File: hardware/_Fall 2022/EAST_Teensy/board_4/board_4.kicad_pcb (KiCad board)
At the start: 2 copper layers, 76.2 x 66.7 mm, 8 parts, among them J1 Conn_01x04, J2 Conn_02x09_Odd_Even, U1 Teensy4.1

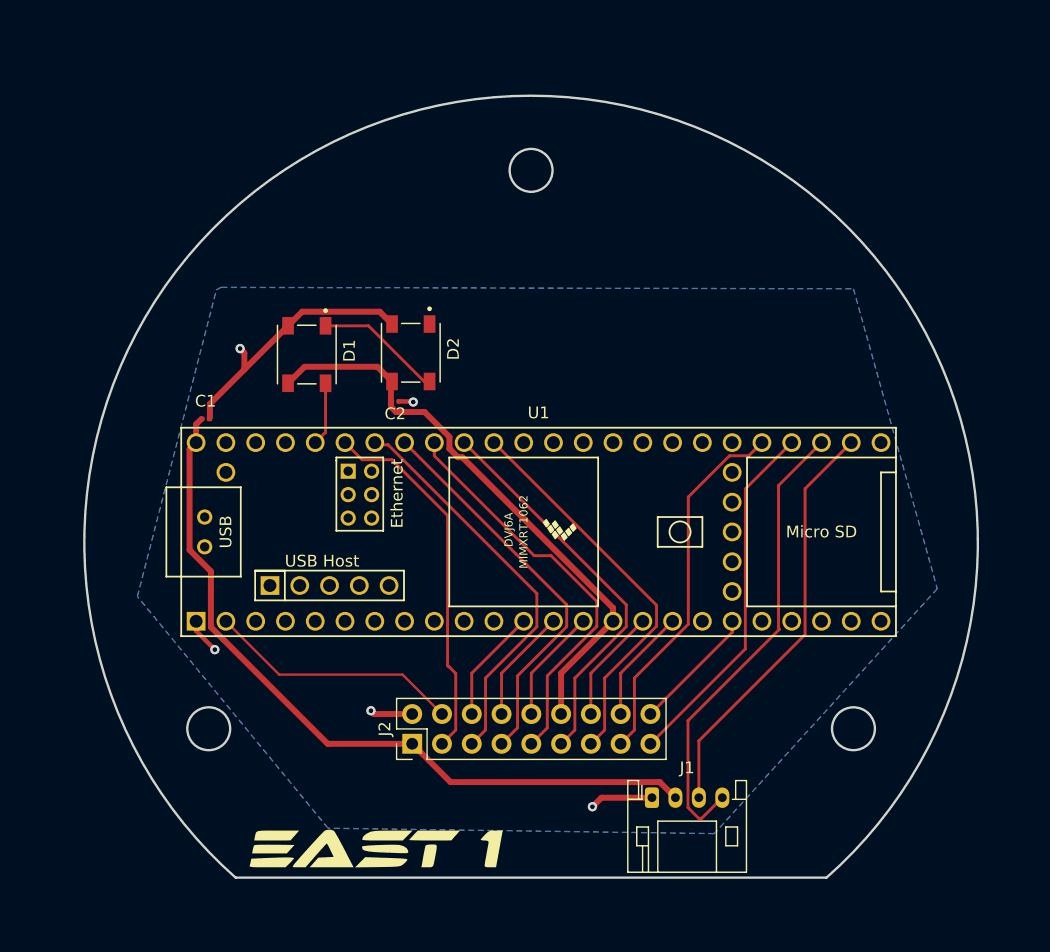
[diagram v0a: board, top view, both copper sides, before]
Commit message: add plated holes to both east boards
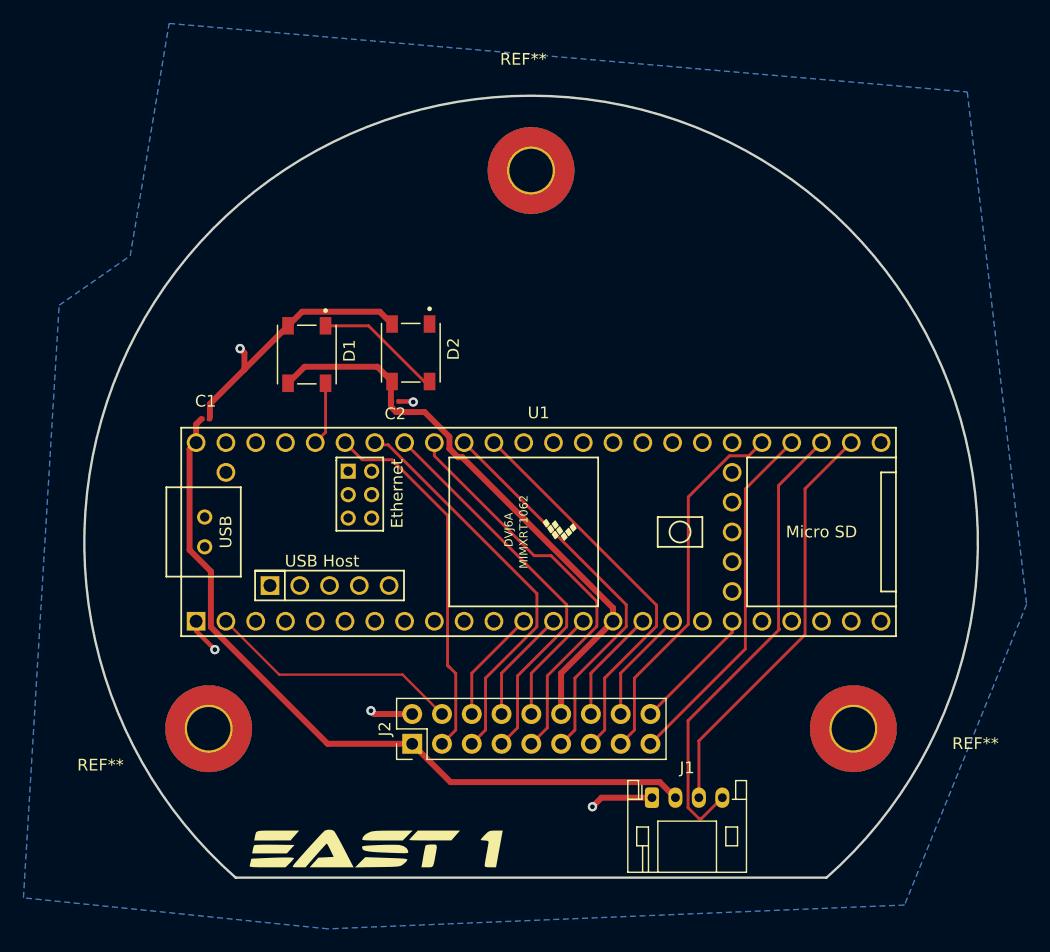
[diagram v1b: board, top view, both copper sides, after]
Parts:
- added REF**: MountingHole_3.7mm_Pad_TopBottom, MountingHole:MountingHole_3.7mm_Pad_TopBottom, F.Cu at (175.5, 139.4)
- added REF**: MountingHole_3.7mm_Pad_TopBottom, MountingHole:MountingHole_3.7mm_Pad_TopBottom, F.Cu at (148.0, 91.8)
- added REF**: MountingHole_3.7mm_Pad_TopBottom, MountingHole:MountingHole_3.7mm_Pad_TopBottom, F.Cu at (120.5, 139.4)
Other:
- outline, holes or cut-outs redrawn
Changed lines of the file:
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@@
   (net 68 "unconnected-(D2-Pad1)")
   (net 69 "unconnected-(U1-Pad23)")
+  (footprint "MountingHole:MountingHole_3.7mm_Pad_TopBottom" (layer "F.Cu")
+    (at 175.468013 139.389531)
+    (descr "Mounting Hole 3.7mm")
+    (tags "mounting hole 3.7mm")
+    (attr exclude_from_pos_files exclude_from_bom)
+    (fp_text reference "REF**" (at 10.414 1.27) (layer "F.SilkS")
+      (effects (font (size 1 1) (thickness 0.15)))
+    )
+    (fp_text value "MountingHole_3.7mm_Pad_TopBottom" (at 0 4.7) (layer "F.Fab")
+      (effects (font (size 1 1) (thickness 0.15)))
+    )
+    (fp_text user "${REFERENCE}" (at 0 0) (layer "F.Fab")
+      (effects (font (size 1 1) (thickness 0.15)))
+    )
+    (fp_circle (center 0 0) (end 3.7 0) (layer "Cmts.User") (width 0.15) (fill none))
+    (fp_circle (center 0 0) (end 3.95 0) (layer "F.CrtYd") (width 0.05) (fill none))
+    (pad "1" thru_hole circle (at 0 0) (size 4.1 4.1) (drill 3.7) (layers *.Cu *.Mask))
+    (pad "1" connect circle (at 0 0) (size 7.4 7.4) (layers "F.Cu" "F.Mask"))
+    (pad "1" connect circle (at 0 0) (size 7.4 7.4) (layers "B.Cu" "B.Mask"))
+  )
   (footprint "LOGO" (layer "F.Cu")
     (at 134.62 149.86)
@@
       (rotate (xyz 0 0 0))
     )
+  )
+  (footprint "MountingHole:MountingHole_3.7mm_Pad_TopBottom" (layer "F.Cu")
+    (at 147.976228 91.782125)
+    (descr "Mounting Hole 3.7mm")
+    (tags "mounting hole 3.7mm")
+    (attr exclude_from_pos_files exclude_from_bom)
+    (fp_text reference "REF**" (at -0.656228 -9.486125) (layer "F.SilkS")
+      (effects (font (size 1 1) (thickness 0.15)))
+    )
+    (fp_text value "MountingHole_3.7mm_Pad_TopBottom" (at 0 4.7) (layer "F.Fab")
+      (effects (font (size 1 1) (thickness 0.15)))
+    )
+    (fp_text user "${REFERENCE}" (at 0 0) (layer "F.Fab")
+      (effects (font (size 1 1) (thickness 0.15)))
+    )
+    (fp_circle (center 0 0) (end 3.7 0) (layer "Cmts.User") (width 0.15) (fill none))
+    (fp_circle (center 0 0) (end 3.95 0) (layer "F.CrtYd") (width 0.05) (fill none))
+    (pad "1" thru_hole circle (at 0 0) (size 4.1 4.1) (drill 3.7) (layers *.Cu *.Mask))
+    (pad "1" connect circle (at 0 0) (size 7.4 7.4) (layers "F.Cu" "F.Mask"))
+    (pad "1" connect circle (at 0 0) (size 7.4 7.4) (layers "B.Cu" "B.Mask"))
   )
   (footprint "Teensy:Teensy41" (layer "F.Cu")
@@
       (net 3 "Net-(D1-Pad1)") (pinfunction "DIN") (pintype "input"))
   )
+  (footprint "MountingHole:MountingHole_3.7mm_Pad_TopBottom" (layer "F.Cu")
+    (at 120.480277 139.392743)
+    (descr "Mounting Hole 3.7mm")
+    (tags "mounting hole 3.7mm")
+    (attr exclude_from_pos_files exclude_from_bom)
+    (fp_text reference "REF**" (at -9.228277 3.101257) (layer "F.SilkS")
+      (effects (font (size 1 1) (thickness 0.15)))
+    )
+    (fp_text value "MountingHole_3.7mm_Pad_TopBottom" (at 0 4.7) (layer "F.Fab")
+      (effects (font (size 1 1) (thickness 0.15)))
+    )
+    (fp_text user "${REFERENCE}" (at 0 0) (layer "F.Fab")
+      (effects (font (size 1 1) (thickness 0.15)))
+    )
+    (fp_circle (center 0 0) (end 3.7 0) (layer "Cmts.User") (width 0.15) (fill none))
+    (fp_circle (center 0 0) (end 3.95 0) (layer "F.CrtYd") (width 0.05) (fill none))
+    (pad "1" thru_hole circle (at 0 0) (size 4.1 4.1) (drill 3.7) (layers *.Cu *.Mask))
+    (pad "1" connect circle (at 0 0) (size 7.4 7.4) (layers "F.Cu" "F.Mask"))
+    (pad "1" connect circle (at 0 0) (size 7.4 7.4) (layers "B.Cu" "B.Mask"))
+  )
   (footprint "Capacitor_SMD:C_0201_0603Metric" (layer "F.Cu")
     (at 120.225 112.975)
@@
     (pad "18" thru_hole oval (at 2.54 20.32 90) (size 1.7 1.7) (drill 1) (layers *.Cu *.Mask)
       (net 9 "/SCK 1") (pinfunction "Pin_18") (pintype "passive"))
-    (model "${KICAD6_3DMODEL_DIR}/Connector_PinHeader_2.54mm.3dshapes/PinHeader_2x09_P2.54mm_Vertical.wrl"
+    (model "${KICAD6_3DMODEL_DIR}/Connector_PinHeader_2.54mm.3dshapes/PinHeader_2x09_P2.54mm_Vertical.wrl" hide
       (offset (xyz 0 0 0))
+      (scale (xyz 1 1 1))
+      (rotate (xyz 0 0 0))
+    )
+    (model "${KICAD6_3DMODEL_DIR}/Connector_PinSocket_2.54mm.3dshapes/PinSocket_2x09_P2.54mm_Vertical.step"
+      (offset (xyz 2.5 0 0))
       (scale (xyz 1 1 1))
       (rotate (xyz 0 0 0))
@@
   (gr_line (start 155.8204 143.4952) (end 166.7204 143.4952) (layer "Dwgs.User") (width 0.2))
   (gr_line (start 159.4104 141.9352) (end 136.5504 136.8552) (layer "Dwgs.User") (width 0.2))
+  (gr_circle (center 175.4759 139.394734) (end 177.3047 139.394734) (layer "Dwgs.User") (width 0.2) (fill none))
   (gr_line (start 166.7204 152.0952) (end 155.8204 152.0952) (layer "Dwgs.User") (width 0.2))
   (gr_line (start 136.5504 136.8552) (end 159.4104 136.8552) (layer "Dwgs.User") (width 0.2))
   (gr_line (start 147.9804 152.0952) (end 147.9804 139.3952) (layer "Dwgs.User") (width 0.2))
+  (gr_circle (center 147.9804 91.771131) (end 149.8092 91.771131) (layer "Dwgs.User") (width 0.2) (fill none))
+  (gr_circle (center 120.4849 139.394734) (end 122.3137 139.394734) (layer "Dwgs.User") (width 0.2) (fill none))
   (gr_line (start 159.4104 136.8552) (end 159.4104 141.9352) (layer "Dwgs.User") (width 0.2))
   (gr_line (start 161.2704 143.4952) (end 161.2704 152.0952) (layer "Dwgs.User") (width 0.2))
-  (gr_circle (center 175.4759 139.394734) (end 177.3047 139.394734) (layer "Edge.Cuts") (width 0.2) (fill none))
   (gr_line (start 122.779619 152.0952) (end 173.181181 152.0952) (layer "Edge.Cuts") (width 0.2))
-  (gr_circle (center 147.9804 91.771131) (end 149.8092 91.771131) (layer "Edge.Cuts") (width 0.2) (fill none))
-  (gr_circle (center 120.4849 139.394734) (end 122.3137 139.394734) (layer "Edge.Cuts") (width 0.2) (fill none))
   (gr_arc (start 122.779619 152.0952) (mid 147.9804 85.403268) (end 173.181181 152.0952) (layer "Edge.Cuts") (width 0.2))
   (segment (start 137.84 140.68) (end 130.626576 140.68) (width 0.508) (layer "F.Cu") (net 1))
@@
   (segment (start 158.16 140.68) (end 166.255 132.585) (width 0.25) (layer "F.Cu") (net 63))
   (zone (net 2) (net_name "GND") (layer "B.Cu") (hatch edge 0.508)
-    (connect_pads (clearance 0.508))
+    (connect_pads (clearance 1))
     (min_thickness 0.254) (filled_areas_thickness no)
     (fill yes (thermal_gap 0.508) (thermal_bridge_width 0.508))
     (polygon
       (pts
-        (xy 121.56 101.75)
-        (xy 175.474371 101.874481)
-        (xy 182.626 127.4572)
-        (xy 163.6 148.34)
-        (xy 130.66 147.88)
-        (xy 114.4016 128.1176)
-        (xy 121.14 101.96)
-        (xy 121.54 101.75)
+        (xy 117.109861 79.239885)
+        (xy 185.181861 85.081885)
+        (xy 190.246 128.778)
+        (xy 179.832 154.432)
+        (xy 130.66 156.464)
+        (xy 104.682416 153.81886)
+        (xy 107.730416 103.27286)
+        (xy 113.792 99.06)
       )
     )

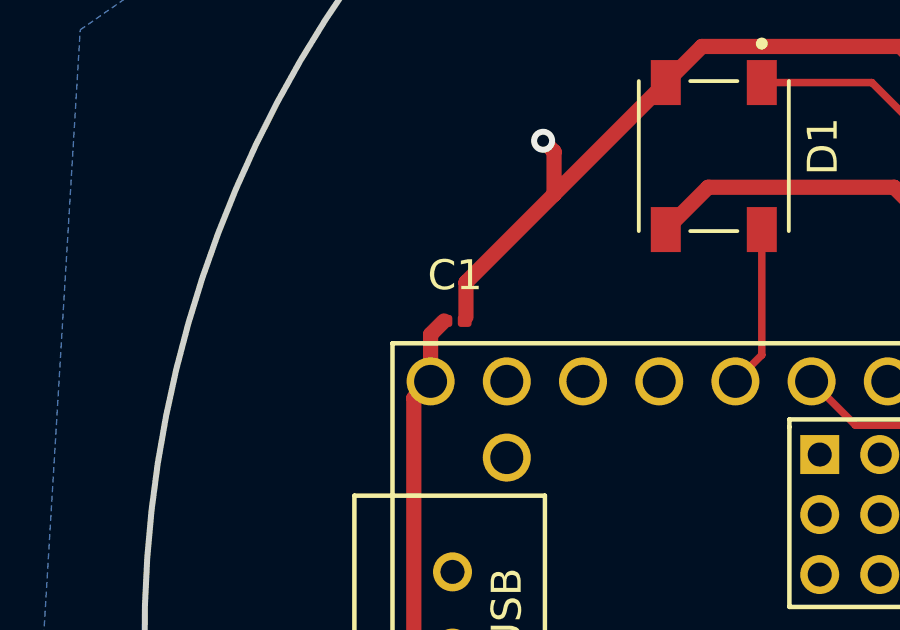
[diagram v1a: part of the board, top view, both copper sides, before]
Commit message: change board 4 C size and GPS labels hided
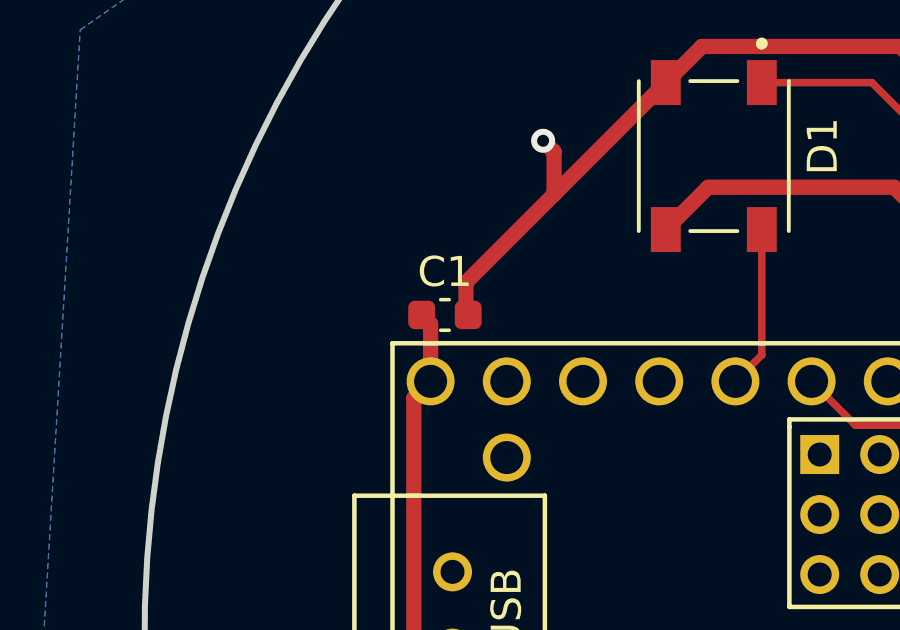
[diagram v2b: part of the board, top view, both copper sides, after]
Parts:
- C1: footprint Capacitor_SMD:C_0201_0603Metric -> Capacitor_SMD:C_0603_1608Metric
- moved C1 0.39 mm to (119.9, 112.8)
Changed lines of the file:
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@@
     (fp_circle (center 0 0) (end 3.7 0) (layer "Cmts.User") (width 0.15) (fill none))
     (fp_circle (center 0 0) (end 3.95 0) (layer "F.CrtYd") (width 0.05) (fill none))
+    (pad "1" connect circle (at 0 0) (size 7.4 7.4) (layers "B.Cu" "B.Mask"))
+    (pad "1" connect circle (at 0 0) (size 7.4 7.4) (layers "F.Cu" "F.Mask"))
     (pad "1" thru_hole circle (at 0 0) (size 4.1 4.1) (drill 3.7) (layers *.Cu *.Mask))
-    (pad "1" connect circle (at 0 0) (size 7.4 7.4) (layers "F.Cu" "F.Mask"))
-    (pad "1" connect circle (at 0 0) (size 7.4 7.4) (layers "B.Cu" "B.Mask"))
   )
   (footprint "Teensy:Teensy41" (layer "F.Cu")
@@
     (fp_circle (center 0 0) (end 3.7 0) (layer "Cmts.User") (width 0.15) (fill none))
     (fp_circle (center 0 0) (end 3.95 0) (layer "F.CrtYd") (width 0.05) (fill none))
+    (pad "1" connect circle (at 0 0) (size 7.4 7.4) (layers "B.Cu" "B.Mask"))
     (pad "1" thru_hole circle (at 0 0) (size 4.1 4.1) (drill 3.7) (layers *.Cu *.Mask))
     (pad "1" connect circle (at 0 0) (size 7.4 7.4) (layers "F.Cu" "F.Mask"))
-    (pad "1" connect circle (at 0 0) (size 7.4 7.4) (layers "B.Cu" "B.Mask"))
-  )
-  (footprint "Capacitor_SMD:C_0201_0603Metric" (layer "F.Cu")
-    (at 120.225 112.975)
-    (descr "Capacitor SMD 0201 (0603 Metric), square (rectangular) end terminal, IPC_7351 nominal, (Body size source: https://www.vishay.com/docs/20052/crcw0201e3.pdf), generated with kicad-footprint-generator")
+  )
+  (footprint "Capacitor_SMD:C_0603_1608Metric" (layer "F.Cu")
+    (at 119.888 112.776)
+    (descr "Capacitor SMD 0603 (1608 Metric), square (rectangular) end terminal, IPC_7351 nominal, (Body size source: IPC-SM-782 page 76, https://www.pcb-3d.com/wordpress/wp-content/uploads/ipc-sm-782a_amendment_1_and_2.pdf), generated with kicad-footprint-generator")
     (tags "capacitor")
     (property "JLC" "C307380")
@@
     (property "Sheetname" "")
     (attr smd)
-    (fp_text reference "C1" (at 0 -1.52) (layer "F.SilkS")
-      (effects (font (size 1 1) (thickness 0.15)))
-    )
-    (fp_text value "0.1uF" (at 0 1.05) (layer "F.Fab")
-      (effects (font (size 1 1) (thickness 0.15)))
-    )
-    (fp_text user "${REFERENCE}" (at 0 -0.68) (layer "F.Fab")
-      (effects (font (size 0.25 0.25) (thickness 0.04)))
-    )
-    (fp_line (start -0.7 -0.35) (end 0.7 -0.35) (layer "F.CrtYd") (width 0.05))
-    (fp_line (start 0.7 0.35) (end -0.7 0.35) (layer "F.CrtYd") (width 0.05))
-    (fp_line (start 0.7 -0.35) (end 0.7 0.35) (layer "F.CrtYd") (width 0.05))
-    (fp_line (start -0.7 0.35) (end -0.7 -0.35) (layer "F.CrtYd") (width 0.05))
-    (fp_line (start 0.3 0.15) (end -0.3 0.15) (layer "F.Fab") (width 0.1))
-    (fp_line (start 0.3 -0.15) (end 0.3 0.15) (layer "F.Fab") (width 0.1))
-    (fp_line (start -0.3 -0.15) (end 0.3 -0.15) (layer "F.Fab") (width 0.1))
-    (fp_line (start -0.3 0.15) (end -0.3 -0.15) (layer "F.Fab") (width 0.1))
-    (pad "" smd roundrect (at -0.345 0) (size 0.318 0.36) (layers "F.Paste") (roundrect_rratio 0.25))
-    (pad "" smd roundrect (at 0.345 0) (size 0.318 0.36) (layers "F.Paste") (roundrect_rratio 0.25))
-    (pad "1" smd roundrect (at -0.32 0) (size 0.46 0.4) (layers "F.Cu" "F.Mask") (roundrect_rratio 0.25)
+    (fp_text reference "C1" (at 0 -1.43) (layer "F.SilkS")
+      (effects (font (size 1 1) (thickness 0.15)))
+    )
+    (fp_text value "0.1uF" (at 0 1.43) (layer "F.Fab")
+      (effects (font (size 1 1) (thickness 0.15)))
+    )
+    (fp_text user "${REFERENCE}" (at 0 0) (layer "F.Fab")
+      (effects (font (size 0.4 0.4) (thickness 0.06)))
+    )
+    (fp_line (start -0.14058 -0.51) (end 0.14058 -0.51) (layer "F.SilkS") (width 0.12))
+    (fp_line (start -0.14058 0.51) (end 0.14058 0.51) (layer "F.SilkS") (width 0.12))
+    (fp_line (start -1.48 0.73) (end -1.48 -0.73) (layer "F.CrtYd") (width 0.05))
+    (fp_line (start 1.48 -0.73) (end 1.48 0.73) (layer "F.CrtYd") (width 0.05))
+    (fp_line (start -1.48 -0.73) (end 1.48 -0.73) (layer "F.CrtYd") (width 0.05))
+    (fp_line (start 1.48 0.73) (end -1.48 0.73) (layer "F.CrtYd") (width 0.05))
+    (fp_line (start 0.8 -0.4) (end 0.8 0.4) (layer "F.Fab") (width 0.1))
+    (fp_line (start 0.8 0.4) (end -0.8 0.4) (layer "F.Fab") (width 0.1))
+    (fp_line (start -0.8 0.4) (end -0.8 -0.4) (layer "F.Fab") (width 0.1))
+    (fp_line (start -0.8 -0.4) (end 0.8 -0.4) (layer "F.Fab") (width 0.1))
+    (pad "1" smd roundrect (at -0.775 0) (size 0.9 0.95) (layers "F.Cu" "F.Paste" "F.Mask") (roundrect_rratio 0.25)
       (net 1 "/V_BATT") (pintype "passive"))
-    (pad "2" smd roundrect (at 0.32 0) (size 0.46 0.4) (layers "F.Cu" "F.Mask") (roundrect_rratio 0.25)
+    (pad "2" smd roundrect (at 0.775 0) (size 0.9 0.95) (layers "F.Cu" "F.Paste" "F.Mask") (roundrect_rratio 0.25)
       (net 2 "GND") (pintype "passive"))
-    (model "${KICAD6_3DMODEL_DIR}/Capacitor_SMD.3dshapes/C_0201_0603Metric.wrl"
+    (model "${KICAD6_3DMODEL_DIR}/Capacitor_SMD.3dshapes/C_0603_1608Metric.wrl"
       (offset (xyz 0 0 0))
       (scale (xyz 1 1 1))
@@
   (segment (start 118.85 124.151292) (end 118.85 115.55) (width 0.508) (layer "F.Cu") (net 1))
   (segment (start 160.29 145.2764) (end 158.961 143.9474) (width 0.508) (layer "F.Cu") (net 1))
+  (segment (start 119.41 113.073) (end 119.113 112.776) (width 0.508) (layer "F.Cu") (net 1))
   (segment (start 118.85 115.55) (end 119.41 114.99) (width 0.508) (layer "F.Cu") (net 1))
   (segment (start 158.961 143.9474) (end 141.1074 143.9474) (width 0.508) (layer "F.Cu") (net 1))
   (segment (start 120.671646 130.72507) (end 120.671646 125.972938) (width 0.508) (layer "F.Cu") (net 1))
-  (segment (start 119.41 113.426) (end 119.861 112.975) (width 0.508) (layer "F.Cu") (net 1))
   (segment (start 130.626576 140.68) (end 120.671646 130.72507) (width 0.508) (layer "F.Cu") (net 1))
-  (segment (start 119.41 114.99) (end 119.41 113.426) (width 0.508) (layer "F.Cu") (net 1))
+  (segment (start 119.41 114.99) (end 119.41 113.073) (width 0.508) (layer "F.Cu") (net 1))
   (segment (start 136.12 104.8775) (end 135.0685 103.826) (width 0.508) (layer "F.Cu") (net 2))
   (segment (start 123.525 107.335) (end 123.16 106.97) (width 0.508) (layer "F.Cu") (net 2))

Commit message: minor fixes
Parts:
- C2: footprint Capacitor_SMD:C_0201_0603Metric -> Capacitor_SMD:C_0603_1608Metric
- moved ? 0.81 mm to (133.8, 149.7)
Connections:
- J1 pad 1: GND -> /TX 0
- J1 pad 2: /V_BATT -> /RX 0
- J1 pad 3: /RX 0 -> /V_BATT
- J1 pad 4: /TX 0 -> GND
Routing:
- net GND: track 35.7 -> 30.1 mm, vias 5 -> 4
- net /V_BATT: track 64.7 -> 69.3 mm
- net /TX 0: track 40.0 -> 36.3 mm
- net /RX 0: track 35.7 -> 36.5 mm
